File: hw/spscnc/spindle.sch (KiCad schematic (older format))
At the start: 32 parts, among them J3 Conn_01x04_Female, Q1 KIA50N06B, Q2 KIA50N06B, Q3 KIA50N06B, Q4 KIA50N06B, U1 IR2104, U2 IR2104

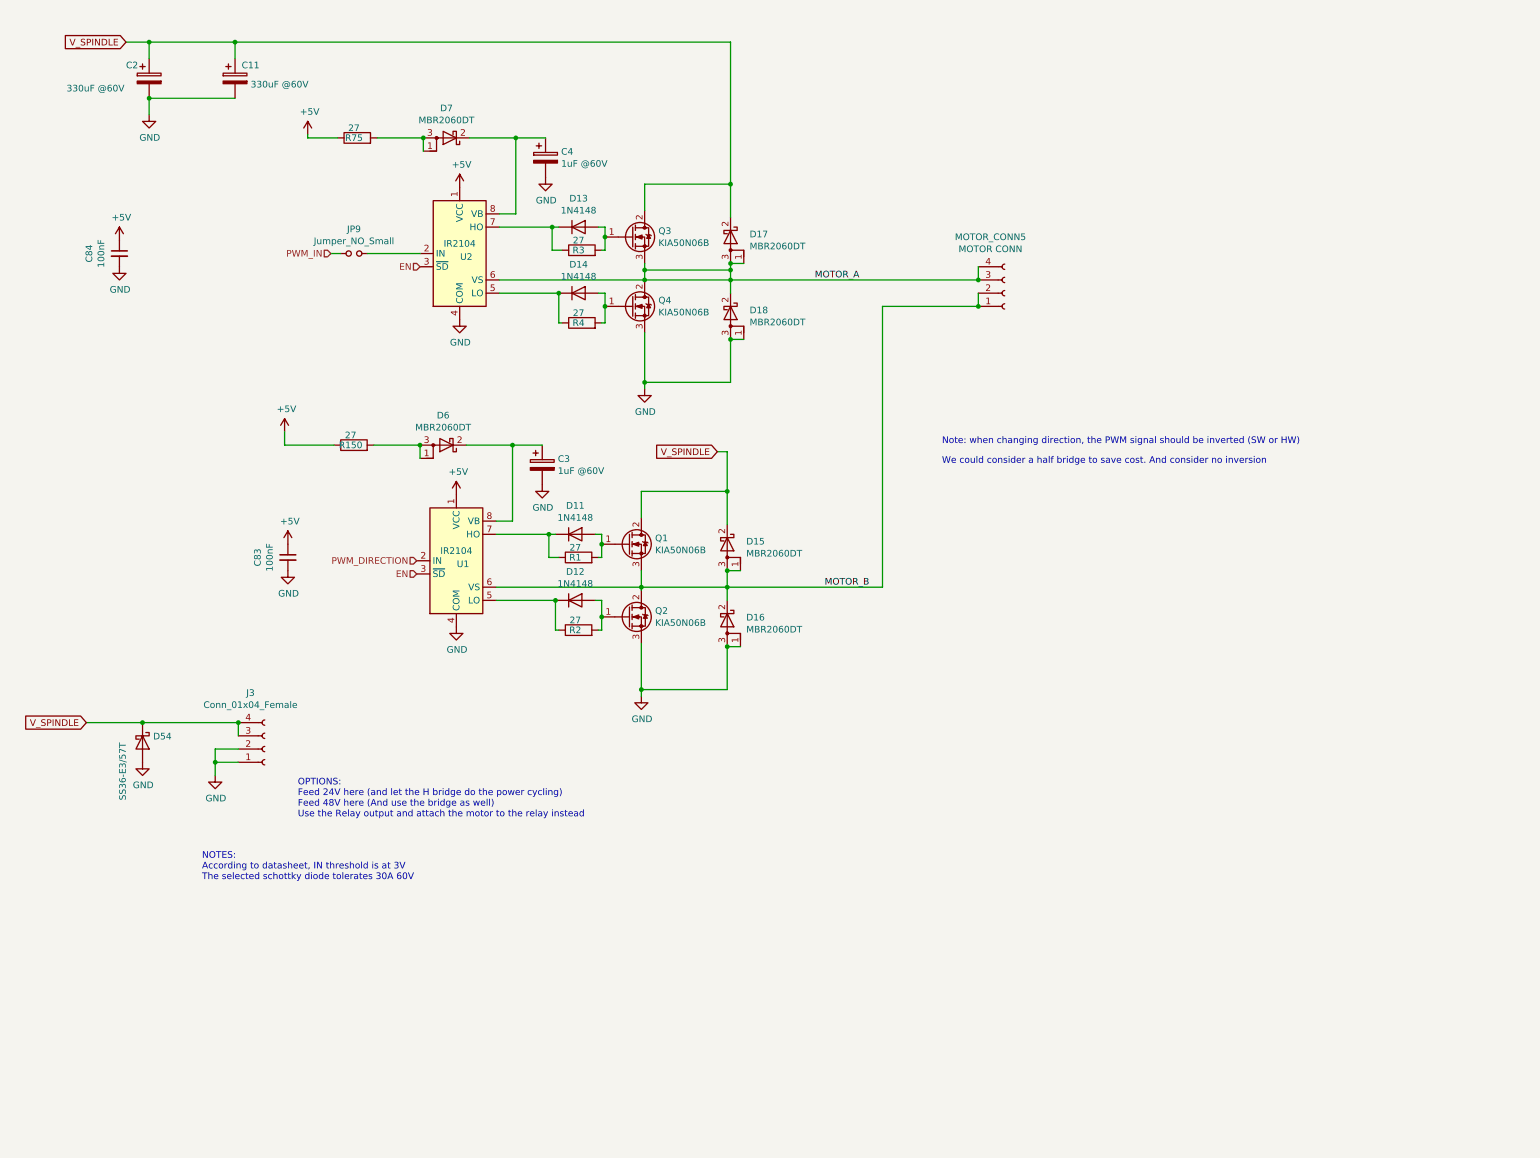
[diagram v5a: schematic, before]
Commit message: Prototype corrections without new PCB
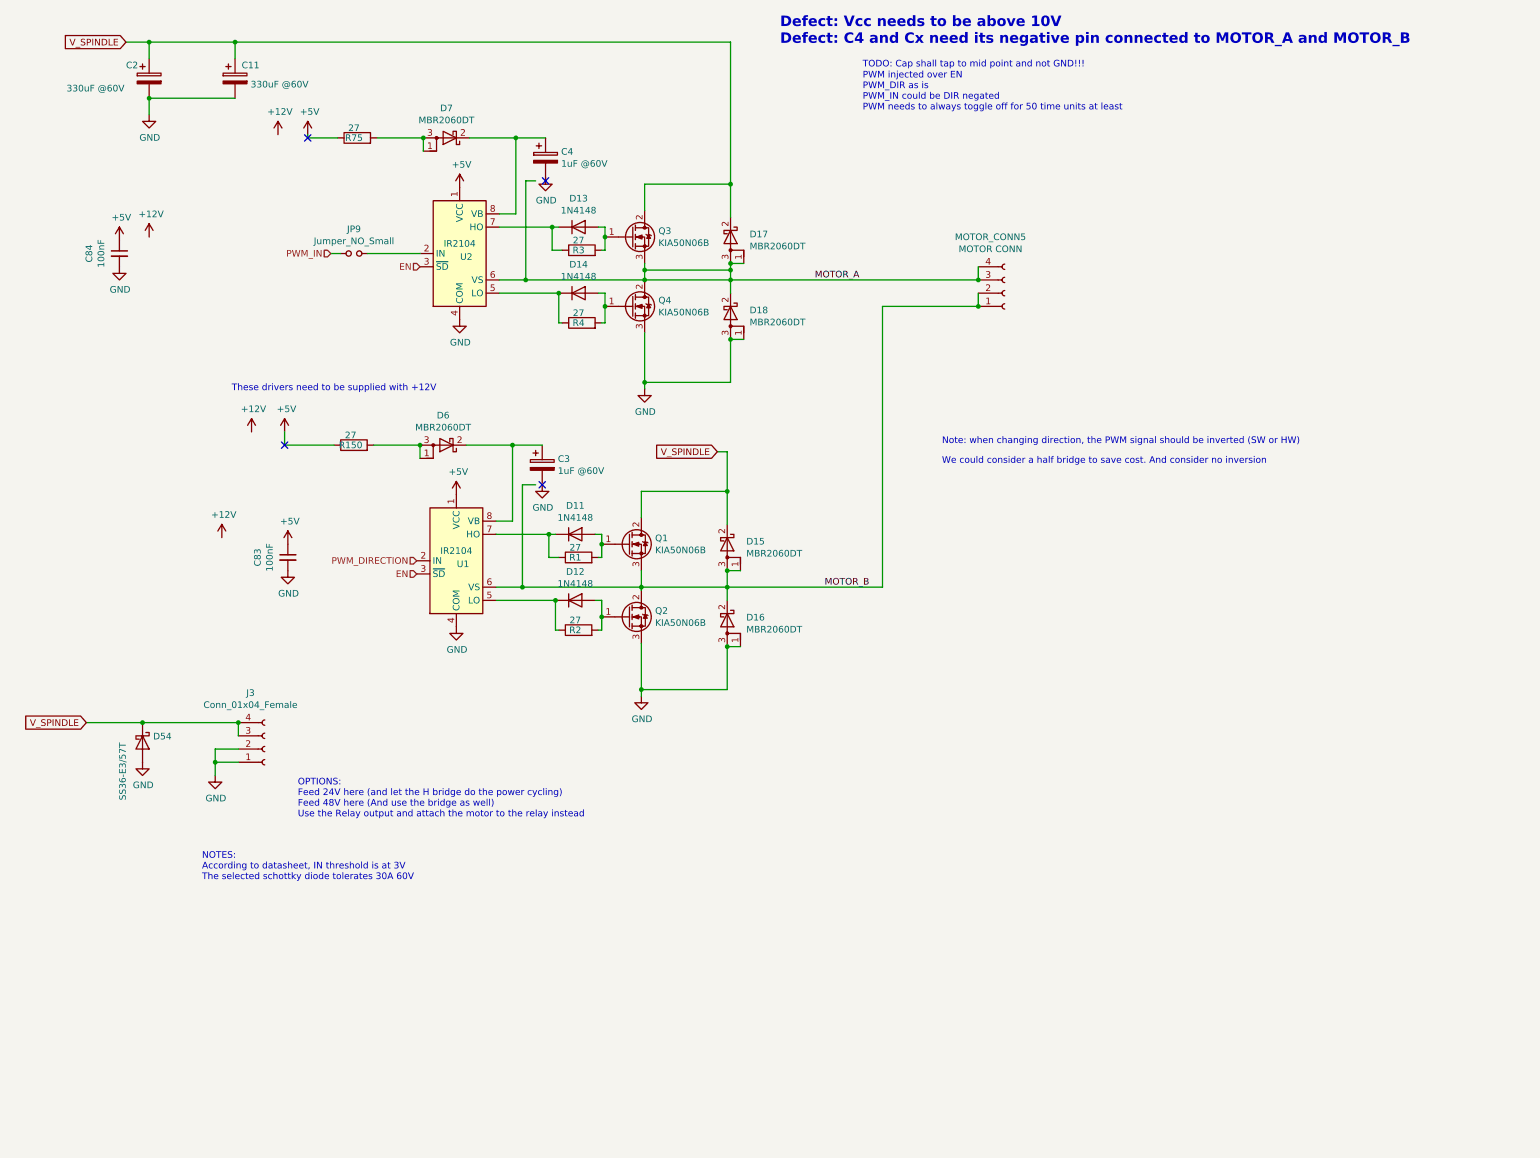
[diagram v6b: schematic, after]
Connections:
- no-connect marks 0 -> 4
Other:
- note added: "Defect: Vcc needs to be above 10V\nDefect: C4 and Cx need its negative pin connected to MOTOR_A and MOTOR_B"
- note added: "PWM injected over EN\nPWM_DIR as is\nPWM_IN could be DIR negated\nPWM needs to always toggle off for 50 time units at least\n"
- note added: "TODO: Cap shall tap to mid point and not GND!!!"
- note added: "These drivers need to be supplied with +12V"
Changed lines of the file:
@@
 Title "Trinamic FluidNC CNC Controller"
 Date "2022-02-12"
-Rev "1.0.1"
+Rev "1.0.2"
 Comp ""
-Comment1 ""
+Comment1 "Corrections implemented in 1.0.1 prototypes."
 Comment2 ""
 Comment3 ""
@@
 	4975 2775 4975 2875
 Wire Wire Line
-	4175 2675 5275 2675
+	4175 2675 4375 2675
 Connection ~ 4975 2875
 Wire Wire Line
@@
 Connection ~ 5275 3450
 Wire Wire Line
-	4150 5000 5250 5000
+	4150 5000 4350 5000
 Connection ~ 4950 5225
 Wire Wire Line
@@
 Wire Wire Line
 	3175 2475 3575 2475
+Text Notes 6925 1075 0    50   ~ 0
+TODO: Cap shall tap to mid point and not GND!!!
+Text Notes 6300 900  0    79   ~ 16
+Defect: Vcc needs to be above 10V\nDefect: C4 and Cx need its negative pin connected to MOTOR_A and MOTOR_B
+Text Notes 6925 1400 0    50   ~ 0
+PWM injected over EN\nPWM_DIR as is\nPWM_IN could be DIR negated\nPWM needs to always toggle off for 50 time units at least\n
+Text Notes 2150 3525 0    50   ~ 0
+These drivers need to be supplied with +12V
+NoConn ~ 4525 1925
+NoConn ~ 4500 4225
+Wire Wire Line
+	4450 1925 4375 1925
+Wire Wire Line
+	4375 1925 4375 2675
+Connection ~ 4375 2675
+Wire Wire Line
+	4375 2675 5275 2675
+Wire Wire Line
+	4450 4225 4350 4225
+Wire Wire Line
+	4350 4225 4350 5000
+Connection ~ 4350 5000
+Wire Wire Line
+	4350 5000 5250 5000
+NoConn ~ 2725 1600
+NoConn ~ 2550 3925
+$Comp
+L power:+12V-power #PWR?
+U 1 1 624E1A1A
+P 2500 1575
+AR Path="/624E1A1A" Ref="#PWR?"  Part="1"
+AR Path="/61C743E7/61A08BFB/624E1A1A" Ref="#PWR?"  Part="1"
+AR Path="/61C80DCB/624E1A1A" Ref="#PWR?"  Part="1"
+F 0 "#PWR?" H 2500 1425 50  0001 C CNN
+F 1 "+12V" H 2515 1748 50  0000 C CNN
+F 2 "" H 2500 1575 50  0001 C CNN
+F 3 "" H 2500 1575 50  0001 C CNN
+	1    2500 1575
+	1    0    0    -1
+$EndComp
+$Comp
+L power:+12V-power #PWR?
+U 1 1 624E5514
+P 2300 3825
+AR Path="/624E5514" Ref="#PWR?"  Part="1"
+AR Path="/61C743E7/61A08BFB/624E5514" Ref="#PWR?"  Part="1"
+AR Path="/61C80DCB/624E5514" Ref="#PWR?"  Part="1"
+F 0 "#PWR?" H 2300 3675 50  0001 C CNN
+F 1 "+12V" H 2315 3998 50  0000 C CNN
+F 2 "" H 2300 3825 50  0001 C CNN
+F 3 "" H 2300 3825 50  0001 C CNN
+	1    2300 3825
+	1    0    0    -1
+$EndComp
+$Comp
+L power:+12V-power #PWR?
+U 1 1 624E5D0C
+P 1525 2350
+AR Path="/624E5D0C" Ref="#PWR?"  Part="1"
+AR Path="/61C743E7/61A08BFB/624E5D0C" Ref="#PWR?"  Part="1"
+AR Path="/61C80DCB/624E5D0C" Ref="#PWR?"  Part="1"
+F 0 "#PWR?" H 1525 2200 50  0001 C CNN
+F 1 "+12V" H 1540 2523 50  0000 C CNN
+F 2 "" H 1525 2350 50  0001 C CNN
+F 3 "" H 1525 2350 50  0001 C CNN
+	1    1525 2350
+	1    0    0    -1
+$EndComp
+$Comp
+L power:+12V-power #PWR?
+U 1 1 624E6475
+P 2075 4625
+AR Path="/624E6475" Ref="#PWR?"  Part="1"
+AR Path="/61C743E7/61A08BFB/624E6475" Ref="#PWR?"  Part="1"
+AR Path="/61C80DCB/624E6475" Ref="#PWR?"  Part="1"
+F 0 "#PWR?" H 2075 4475 50  0001 C CNN
+F 1 "+12V" H 2090 4798 50  0000 C CNN
+F 2 "" H 2075 4625 50  0001 C CNN
+F 3 "" H 2075 4625 50  0001 C CNN
+	1    2075 4625
+	1    0    0    -1
+$EndComp
 $EndSCHEMATC

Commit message: Final HW 1.0.1 corrections and straps. All pending corrections will take place as HW 1.1.0 as those require a new PCB
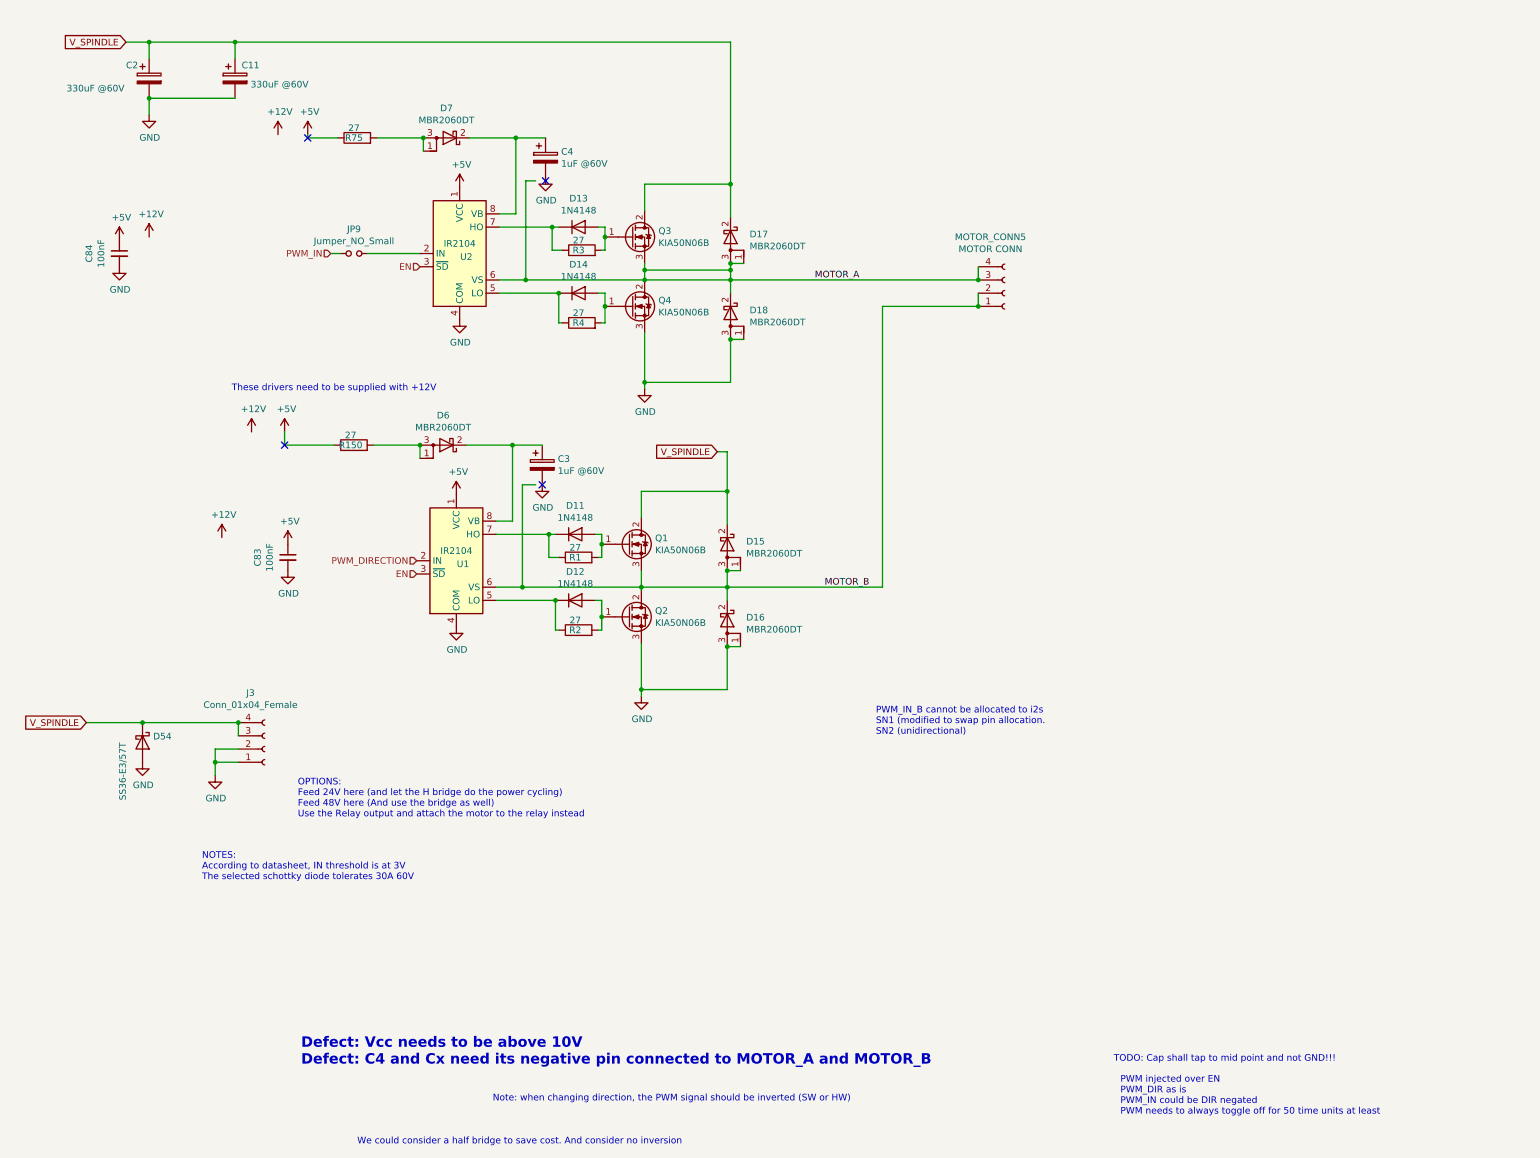
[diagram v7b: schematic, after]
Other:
- note added: "PWM_IN_B cannot be allocated to i2s\nSN1 (modified to swap pin allocation.\nSN2 (unidirectional)"
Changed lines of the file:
@@
 	0    -1   -1   0
 $EndComp
-Text Notes 7525 4075 0    50   ~ 0
+Text Notes 3100 9225 0    50   ~ 0
 We could consider a half bridge to save cost. And consider no inversion
 $Comp
@@
 Wire Wire Line
 	2550 3925 2925 3925
-Text Notes 7525 3925 0    50   ~ 0
+Text Notes 4125 8900 0    50   ~ 0
 Note: when changing direction, the PWM signal should be inverted (SW or HW)
 $Comp
@@
 Wire Wire Line
 	3175 2475 3575 2475
-Text Notes 6925 1075 0    50   ~ 0
+Text Notes 8825 8600 0    50   ~ 0
 TODO: Cap shall tap to mid point and not GND!!!
-Text Notes 6300 900  0    79   ~ 16
+Text Notes 2675 8625 0    79   ~ 16
 Defect: Vcc needs to be above 10V\nDefect: C4 and Cx need its negative pin connected to MOTOR_A and MOTOR_B
-Text Notes 6925 1400 0    50   ~ 0
+Text Notes 8875 9000 0    50   ~ 0
 PWM injected over EN\nPWM_DIR as is\nPWM_IN could be DIR negated\nPWM needs to always toggle off for 50 time units at least\n
 Text Notes 2150 3525 0    50   ~ 0
@@
 	1    0    0    -1
 $EndComp
+Text Notes 7025 6125 0    50   ~ 0
+PWM_IN_B cannot be allocated to i2s\nSN1 (modified to swap pin allocation.\nSN2 (unidirectional)
 $EndSCHEMATC

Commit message: Revision 1.1.0 With only critical corrections. Pending some work on the relays as that part could be remade from scratch for flexibility.
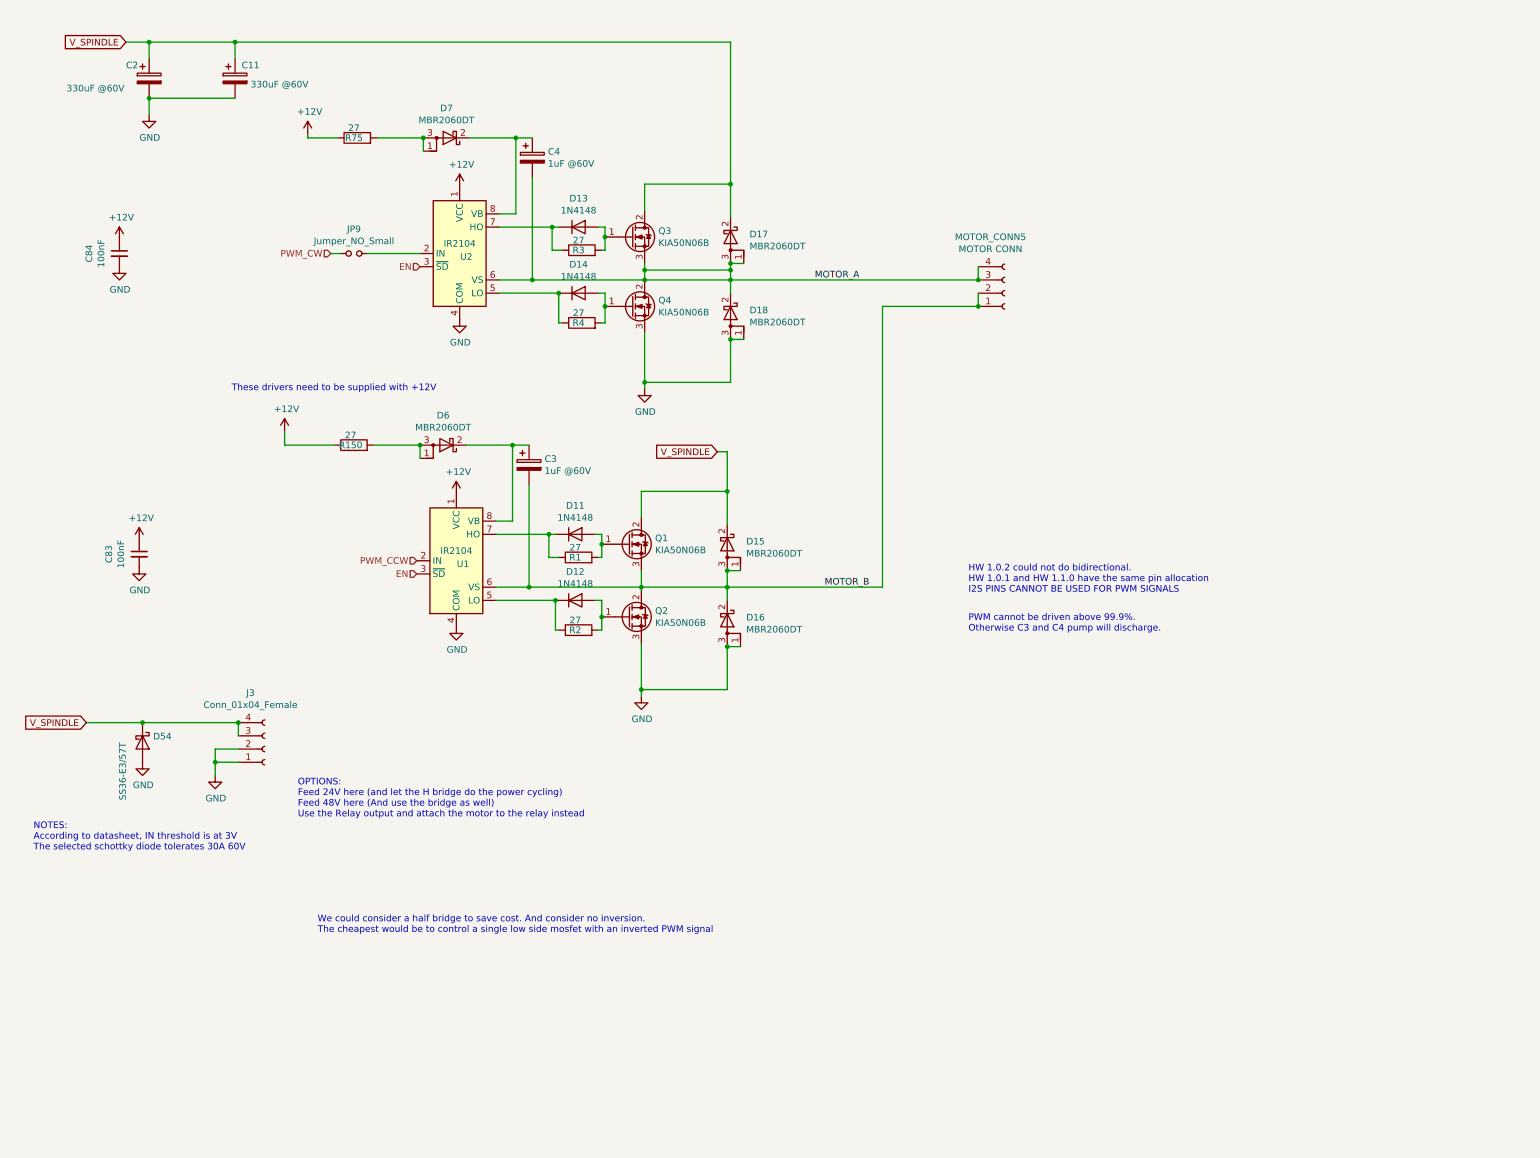
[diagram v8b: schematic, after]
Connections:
- net +5V is gone; now on net +12V: C83.1, C84.1, R150.1, R75.1, U1.1 (VCC), U2.1 (VCC)
- net GND: no longer C3.2, C4.2
- net MOTOR_A: now also C4.2
- net MOTOR_B: now also C3.2
- net PWM_DIRECTION renamed PWM_CCW
- net PWM_IN renamed PWM_CW
- no-connect marks 4 -> 0
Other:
- note added: "HW 1.0.2 could not do bidirectional.\nHW 1.0.1 and HW 1.1.0 have the same pin allocation\nI2S PINS CANNOT BE USED FOR PWM SIGNALS\n"
- note added: "PWM cannot be driven above 99.9%.\nOtherwise C3 and C4 pump will discharge.\n\n"
- note added: "We could consider a half bridge to save cost. And consider no inversion.\nThe cheapest would be to control a single low side mosfet with an inverted PWM signal"
- note removed: "Defect: Vcc needs to be above 10V\nDefect: C4 and Cx need its negative pin connected to MOTOR_A and MOTOR_B"
- note removed: "Note: when changing direction, the PWM signal should be inverted (SW or HW)"
- note removed: "PWM injected over EN\nPWM_DIR as is\nPWM_IN could be DIR negated\nPWM needs to always toggle off for 50 time units at least\n"
- note removed: "PWM_IN_B cannot be allocated to i2s\nSN1 (modified to swap pin allocation.\nSN2 (unidirectional)"
- note removed: "TODO: Cap shall tap to mid point and not GND!!!"
- note removed: "We could consider a half bridge to save cost. And consider no inversion"
- moved on the sheet: C3, C4, C83
